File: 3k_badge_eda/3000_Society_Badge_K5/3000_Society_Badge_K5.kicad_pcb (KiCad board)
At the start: 2 copper layers, 1 part, among them IC1 Trinket3v3

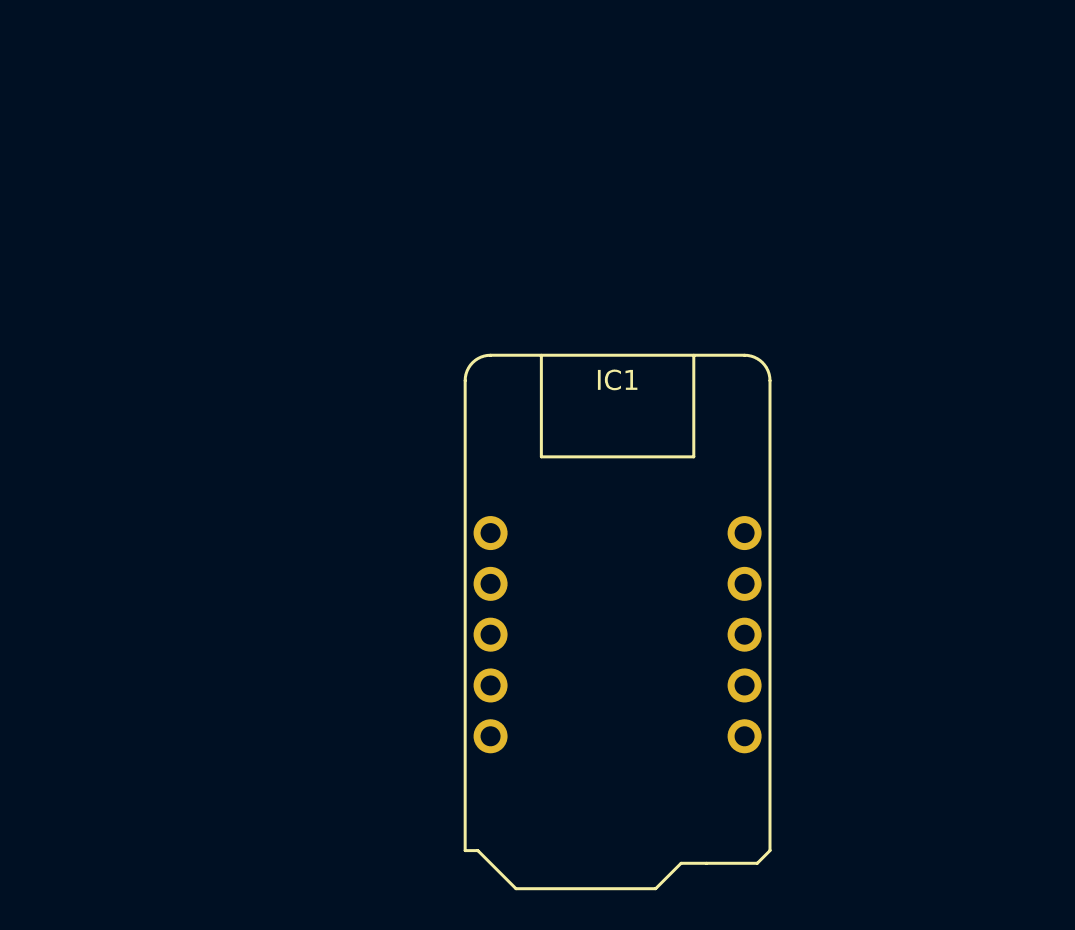
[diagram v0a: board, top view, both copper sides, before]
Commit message: KiCad part schematic and footprint definitions
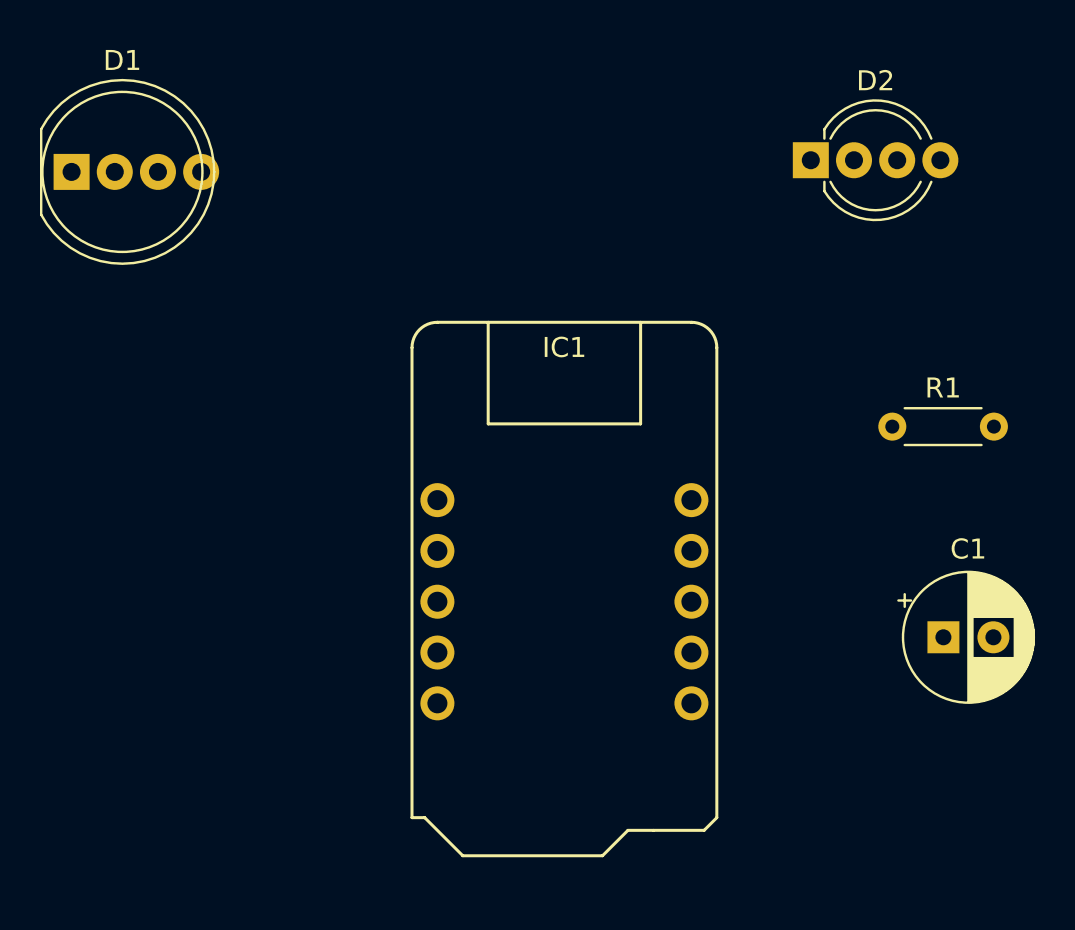
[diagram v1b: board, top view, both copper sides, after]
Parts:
- added C1: CP 100uf, 3000_Society_Badge:CP_Radial_D6.3mm_P2.50mm, F.Cu at (175.5, 91.6)
- added D1: LED_NeoPixel_THT_8mm, 3000_Society_Badge:LED_D8.0mm-4_RGB, F.Cu at (131.9, 68.4)
- added D2: LED_NeoPixel_THT_5mm, 3000_Society_Badge:LED_D5.0mm-4_RGB_Wide_Pins, F.Cu at (168.9, 67.8)
- added R1: R 200ohm, 3000_Society_Badge:R_Axial_DIN0204_L3.6mm_D1.6mm_P5.08mm_Horizontal, F.Cu at (172.9, 81.1)
- IC1: value Trinket3v3 -> Trinket_M0; footprint 3000_Society_Badge:Trinket_3v3 -> 3000_Society_Badge:Trinket_M0
- moved IC1 3.13 mm to (156.5, 75.9)

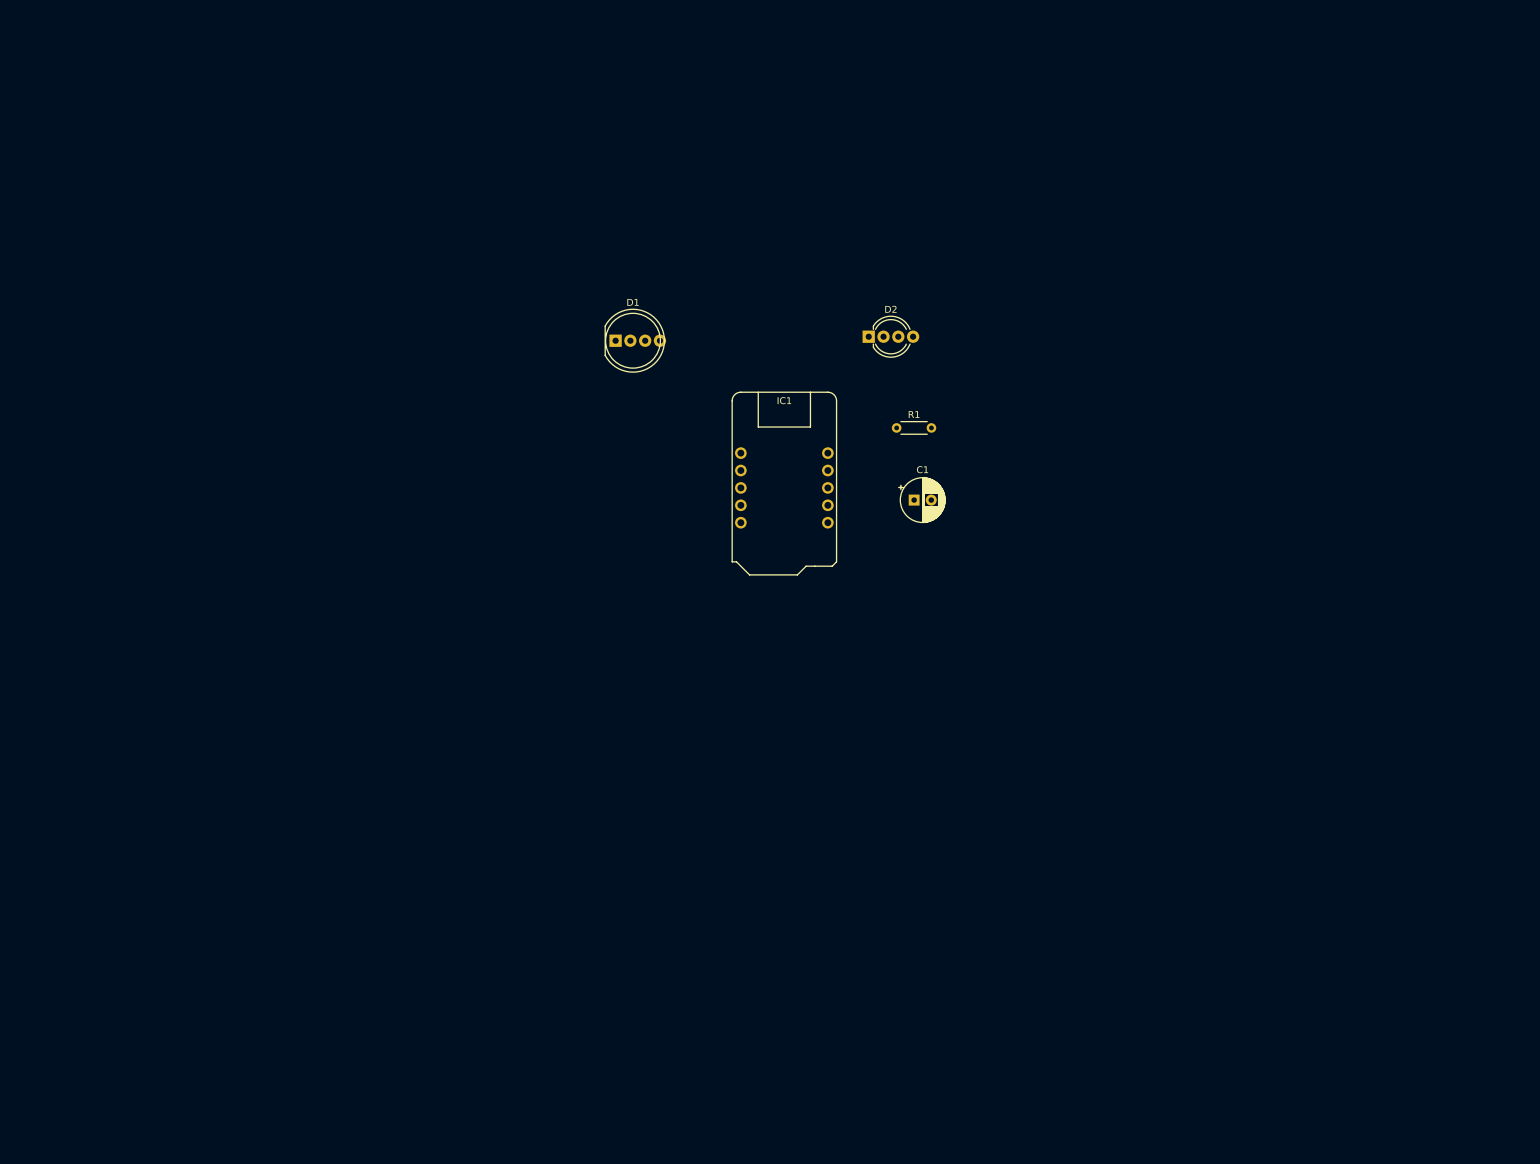
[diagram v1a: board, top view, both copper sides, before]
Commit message: Graphic export and KiCad import tasks
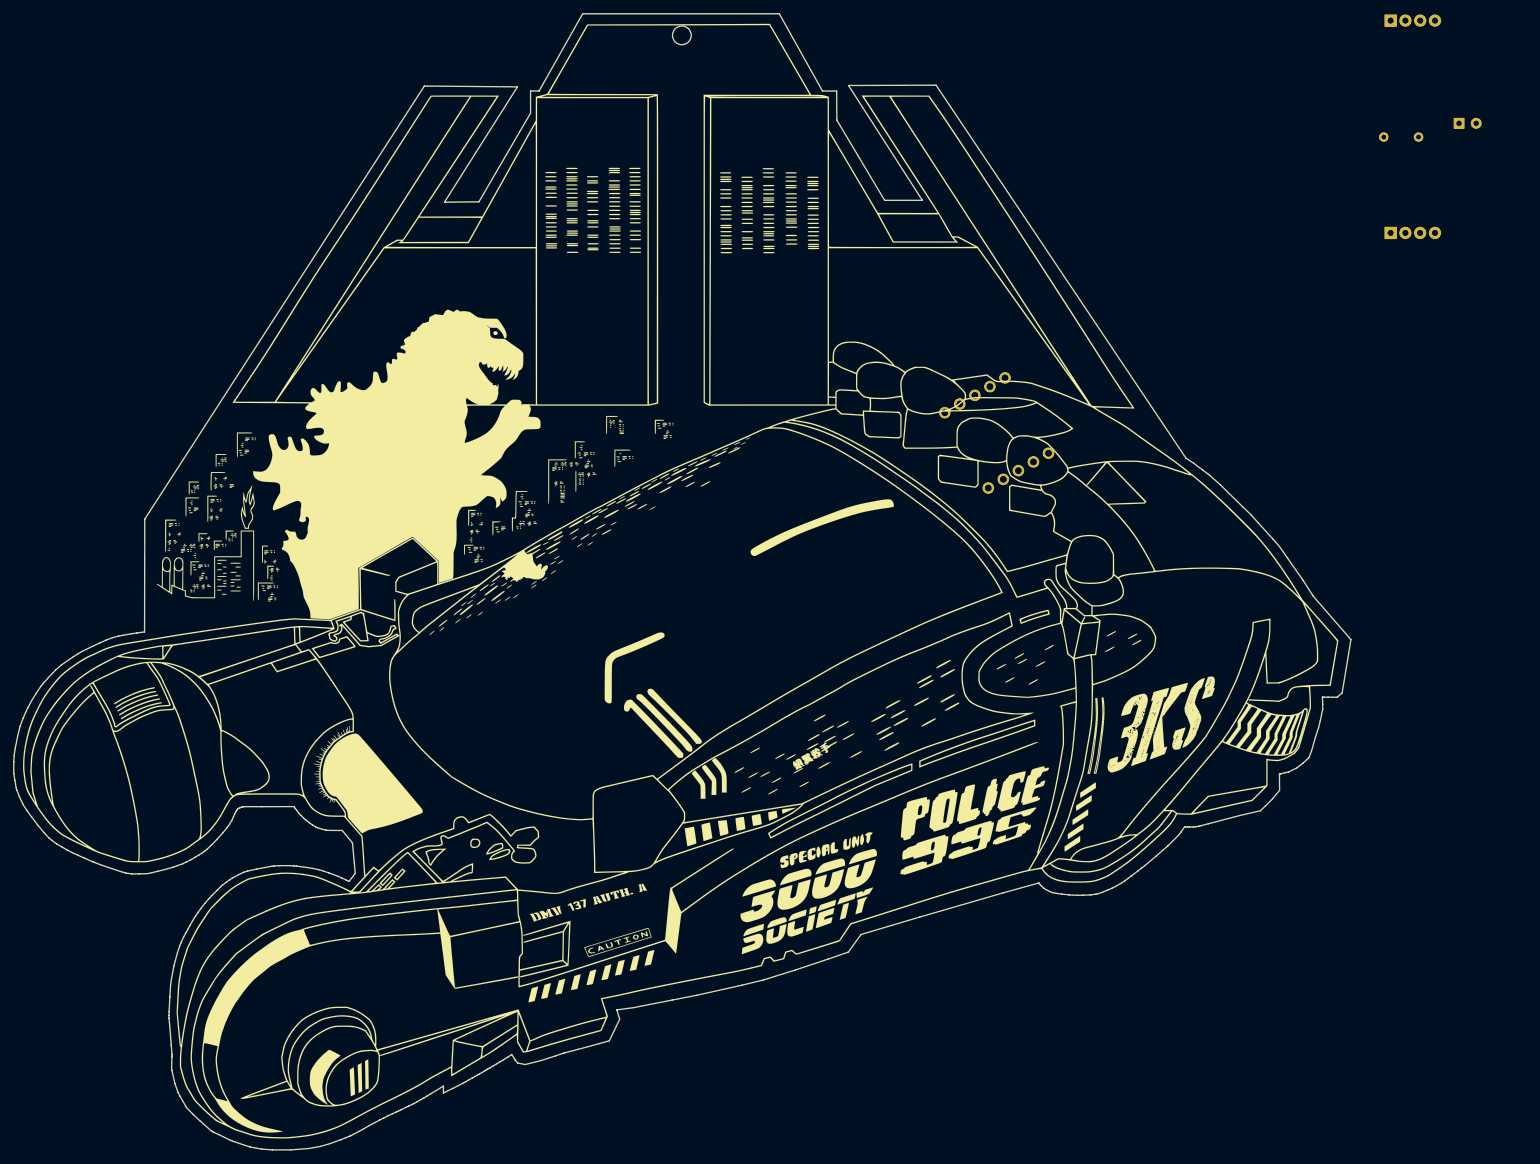
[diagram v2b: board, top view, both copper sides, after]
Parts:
- added Art: , 3000_Society_Badge:3kbadge-for-export-v4-FrontSilk, F.Cu at (141.4, 103.5)
- D1: value LED_NeoPixel_THT_8mm -> LED_NeoPixel_THT_5mm; footprint 3000_Society_Badge:LED_D8.0mm-4_RGB -> 3000_Society_Badge:LED_D5.0mm-4_RGB_Wide_Pins
- D2: value LED_NeoPixel_THT_5mm -> LED_NeoPixel_THT_8mm; footprint 3000_Society_Badge:LED_D5.0mm-4_RGB_Wide_Pins -> 3000_Society_Badge:LED_D8.0mm-4_RGB
- R1: value R 200ohm -> R 220ohm
- moved D1 114.2 mm to (245.1, 52.6)
- moved C1 96.7 mm to (255.1, 36.6)
- moved D2 89.1 mm to (245.1, 21.6)
- moved R1 82.8 mm to (244.1, 38.6)
- moved IC1 43.1 mm to (199.6, 74.9), turned to 300 degrees
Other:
- board outline added: 195.2 x 165.9 mm

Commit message: PCB-updates
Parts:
- removed C1: CP 100uf, 3000_Society_Badge:CP_Radial_D6.3mm_P2.50mm
- removed D1: LED_NeoPixel_THT_5mm, 3000_Society_Badge:LED_D5.0mm-4_RGB_Wide_Pins
- removed D2: LED_NeoPixel_THT_8mm, 3000_Society_Badge:LED_D8.0mm-4_RGB
- removed R1: R 220ohm, 3000_Society_Badge:R_Axial_DIN0204_L3.6mm_D1.6mm_P5.08mm_Horizontal
- added C01: CP 100uF, 3000_Society_Badge:CP_Radial_D6.3mm_P2.50mm, F.Cu at (243.8, 118.1)
- added C02: CP 100uF, 3000_Society_Badge:CP_Radial_D6.3mm_P2.50mm, F.Cu at (234.9, 147.3)
- added C03: CP 100uF, 3000_Society_Badge:CP_Radial_D6.3mm_P2.50mm, F.Cu at (237.5, 57.1)
- added C04: CP 100uF, 3000_Society_Badge:CP_Radial_D6.3mm_P2.50mm, F.Cu at (260.4, 54.6)
- added C05: CP 100uF, 3000_Society_Badge:CP_Radial_D6.3mm_P2.50mm, F.Cu at (221.0, 48.3)
- added D10: LED_NeoPixel_THT_5mm, 3000_Society_Badge:LED_D5.0mm-4_RGB_Wide_Pins, F.Cu at (118.5, 80.2)
- added D11: LED_NeoPixel_THT_5mm, 3000_Society_Badge:LED_D5.0mm-4_RGB_Wide_Pins, F.Cu at (123.3, 84.8)
- added D12: LED_NeoPixel_THT_5mm, 3000_Society_Badge:LED_D5.0mm-4_RGB_Wide_Pins, F.Cu at (130.3, 85.3)
- added D13: LED_NeoPixel_THT_5mm, 3000_Society_Badge:LED_D5.0mm-4_RGB_Wide_Pins, F.Cu at (124.0, 91.6)
- added D20: LED_NeoPixel_THT_8mm, 3000_Society_Badge:LED_D8.0mm-4_RGB, F.Cu at (198.7, 92.0)
- added D21: LED_NeoPixel_THT_5mm, 3000_Society_Badge:LED_D5.0mm-4_RGB_Wide_Pins, F.Cu at (190.8, 95.9)
- added D22: LED_NeoPixel_THT_5mm, 3000_Society_Badge:LED_D5.0mm-4_RGB_Wide_Pins, F.Cu at (197.6, 100.3)
- added D40: LED_NeoPixel_THT_8mm, 3000_Society_Badge:LED_D8.0mm-4_RGB, F.Cu at (171.0, 74.9)
- added D41: LED_NeoPixel_THT_5mm, 3000_Society_Badge:LED_D5.0mm-4_RGB_Wide_Pins, F.Cu at (161.9, 78.6)
- added D42: LED_NeoPixel_THT_5mm, 3000_Society_Badge:LED_D5.0mm-4_RGB_Wide_Pins, F.Cu at (168.1, 82.8)
- added R01: R 470ohm, 3000_Society_Badge:R_Axial_DIN0204_L3.6mm_D1.6mm_P5.08mm_Horizontal, F.Cu at (243.8, 108.0)
- added R02: R 470ohm, 3000_Society_Badge:R_Axial_DIN0204_L3.6mm_D1.6mm_P5.08mm_Horizontal, F.Cu at (238.8, 135.9)
- added R03: R 470ohm, 3000_Society_Badge:R_Axial_DIN0204_L3.6mm_D1.6mm_P5.08mm_Horizontal, F.Cu at (228.6, 63.5)
- added R04: R 470ohm, 3000_Society_Badge:R_Axial_DIN0204_L3.6mm_D1.6mm_P5.08mm_Horizontal, F.Cu at (255.3, 62.2)
- added R05: R 470ohm, 3000_Society_Badge:R_Axial_DIN0204_L3.6mm_D1.6mm_P5.08mm_Horizontal, F.Cu at (226.1, 43.2)
- added R10: R 470ohm, 3000_Society_Badge:R_Axial_DIN0204_L3.6mm_D1.6mm_P5.08mm_Horizontal, F.Cu at (259.1, 106.7)
- added R20: R 470ohm, 3000_Society_Badge:R_Axial_DIN0204_L3.6mm_D1.6mm_P5.08mm_Horizontal, F.Cu at (257.8, 71.1)
- added R40: R 470ohm, 3000_Society_Badge:R_Axial_DIN0204_L3.6mm_D1.6mm_P5.08mm_Horizontal, F.Cu at (222.2, 31.8)
- moved IC1 1.79 mm to (197.8, 75.0), turned to 310 degrees
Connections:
- IC1 pad 10: (no net) -> Net-(IC1-Pad10)
- IC1 pad 2: (no net) -> Net-(C01-Pad2)
- IC1 pad 3: (no net) -> Net-(IC1-Pad3)
- IC1 pad 7: (no net) -> Net-(IC1-Pad7)
- IC1 pad 8: (no net) -> Net-(IC1-Pad8)
